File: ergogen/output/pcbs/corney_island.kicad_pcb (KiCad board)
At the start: 2 copper layers, 134.2 x 92.7 mm, 46 parts

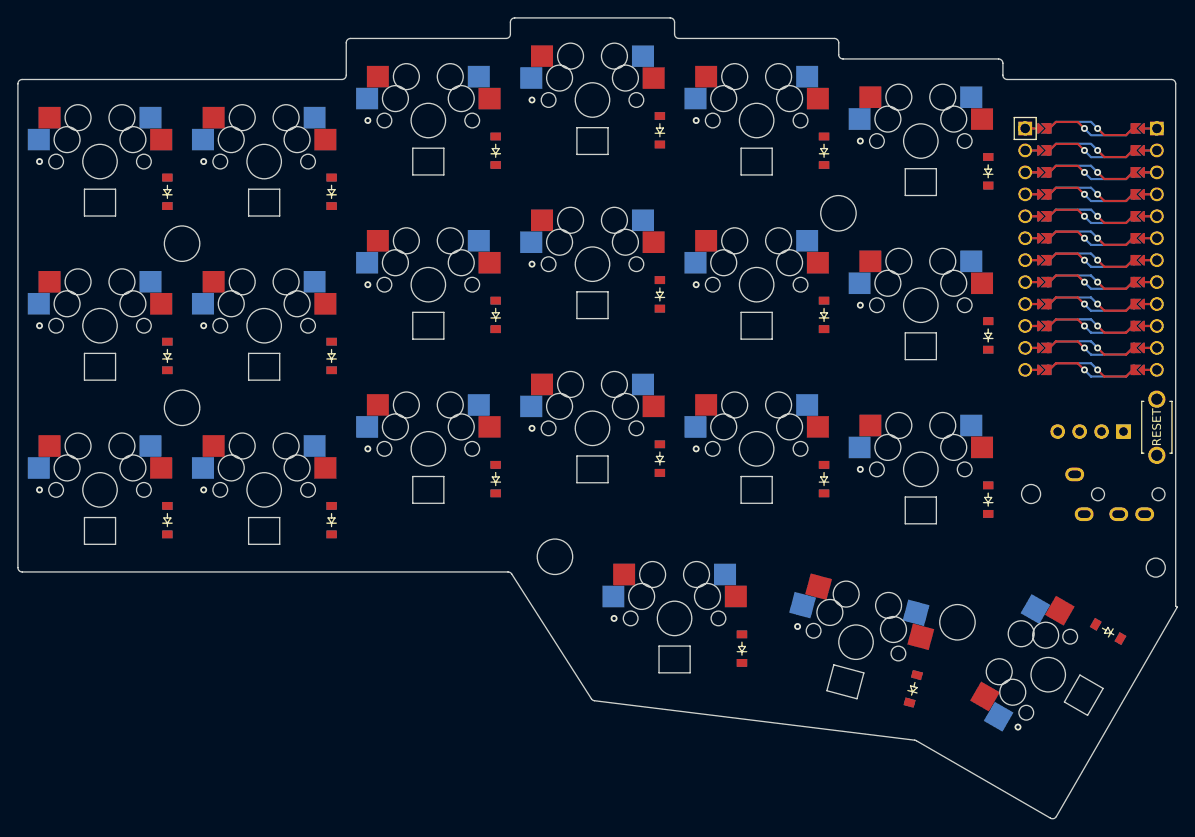
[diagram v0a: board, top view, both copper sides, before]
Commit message: Update nets and diode positions
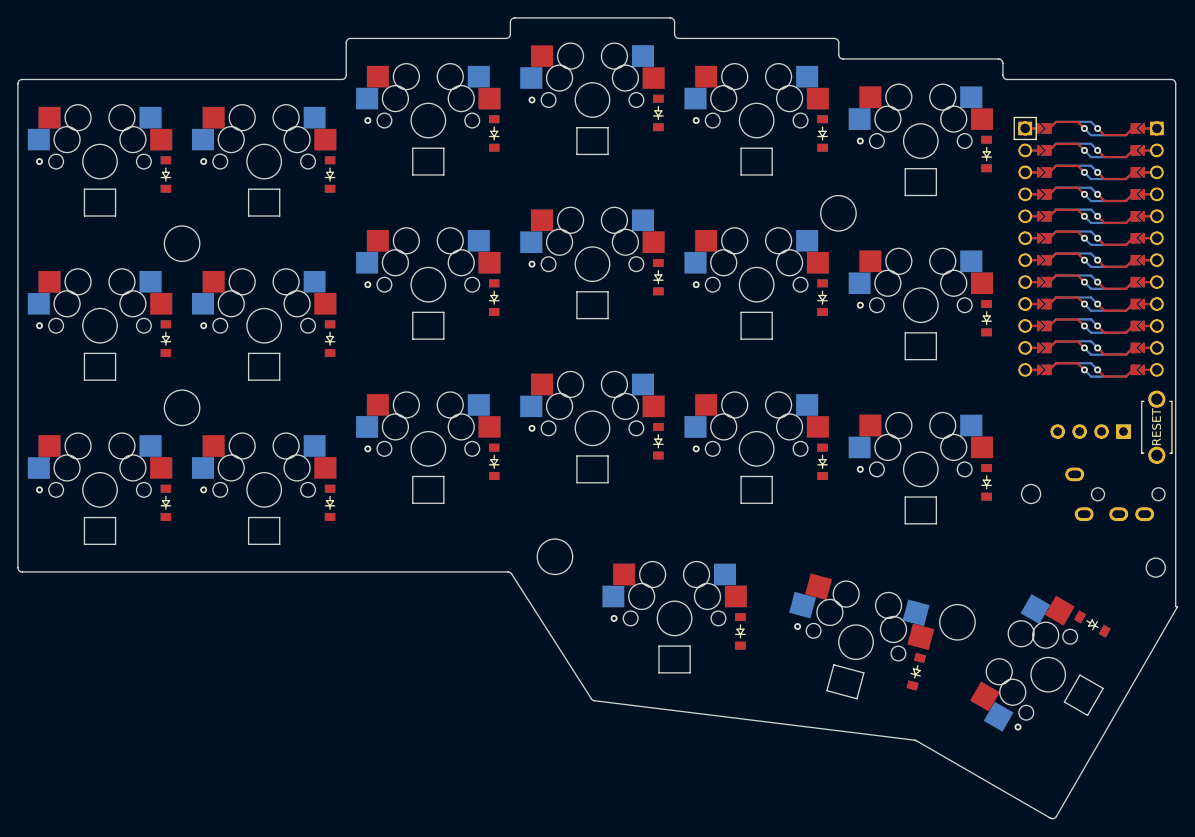
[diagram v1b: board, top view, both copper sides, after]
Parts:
- moved D21 2.01 mm to (214.9, 115.5)
- moved D1 2.01 mm to (107.6, 101.5)
- moved D10 2.01 mm to (164.6, 94.4)
- moved D11 2.01 mm to (164.6, 75.4)
- moved D12 2.01 mm to (164.6, 56.4)
- moved D13 2.01 mm to (183.6, 96.8)
- moved D14 2.01 mm to (183.6, 77.8)
- moved D15 2.01 mm to (183.6, 58.8)
- moved D16 2.01 mm to (202.6, 99.1)
- moved D17 2.01 mm to (202.6, 80.1)
- moved D18 2.01 mm to (202.6, 61.1)
- moved D19 2.01 mm to (174.1, 116.4)
- moved D2 2.01 mm to (107.6, 82.5)
- moved D3 2.01 mm to (107.6, 63.5)
- moved D4 2.01 mm to (126.6, 101.5)
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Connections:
- net P1 renamed LED
- D1 pad 1: R0 -> R2
- D10 pad 1: R0 -> R2
- D12 pad 1: R2 -> R0
- D13 pad 1: R0 -> R2
- D15 pad 1: R2 -> R0
- D16 pad 1: R0 -> R2
- D18 pad 1: R2 -> R0
- D3 pad 1: R2 -> R0
- D4 pad 1: R0 -> R2
- D6 pad 1: R2 -> R0
- D7 pad 1: R0 -> R2
- D9 pad 1: R2 -> R0

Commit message: Add per-key reversible LEDs
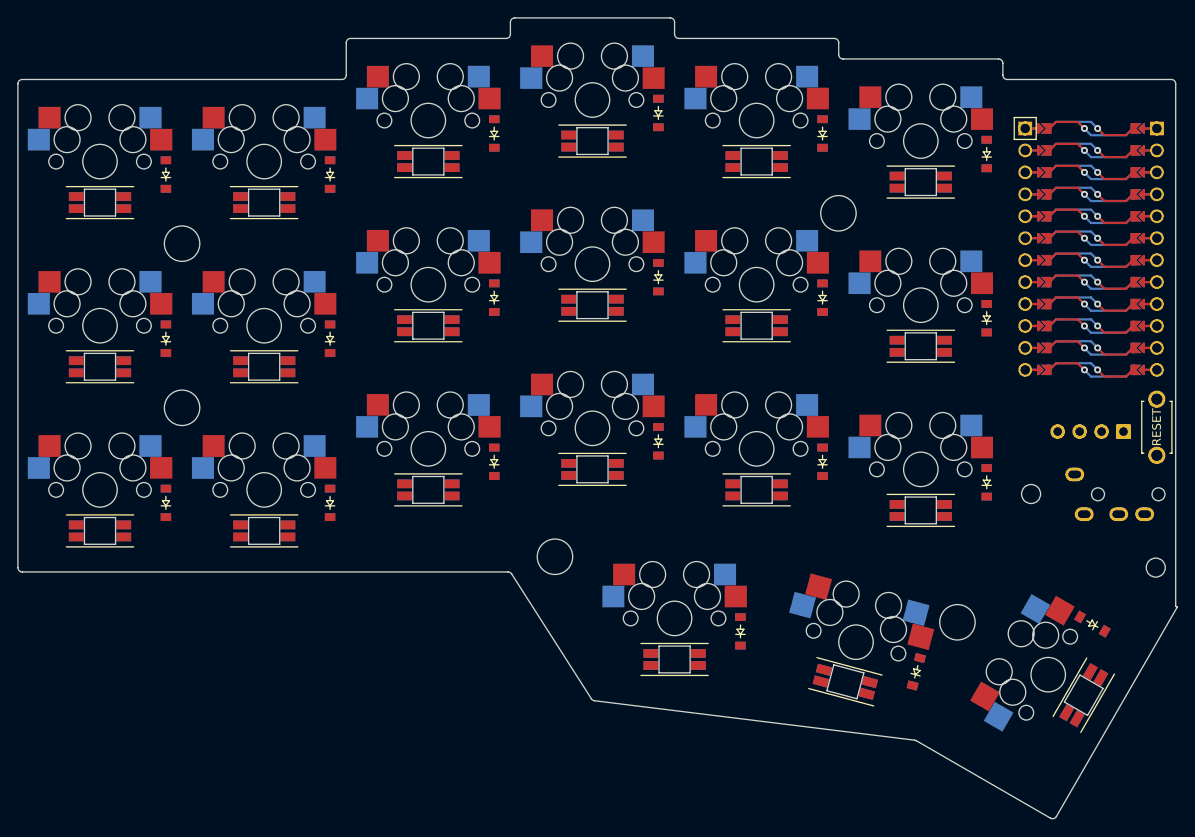
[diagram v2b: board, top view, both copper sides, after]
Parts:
- added LED1: YS-SK6812MINI-E, YS-SK6812MINI-E, F.Cu at (100.0, 104.8)
- added LED10: YS-SK6812MINI-E, YS-SK6812MINI-E, F.Cu at (157.0, 97.6)
- added LED11: YS-SK6812MINI-E, YS-SK6812MINI-E, F.Cu at (157.0, 78.6)
- added LED12: YS-SK6812MINI-E, YS-SK6812MINI-E, F.Cu at (157.0, 59.6)
- added LED13: YS-SK6812MINI-E, YS-SK6812MINI-E, F.Cu at (176.0, 100.0)
- added LED14: YS-SK6812MINI-E, YS-SK6812MINI-E, F.Cu at (176.0, 81.0)
- added LED15: YS-SK6812MINI-E, YS-SK6812MINI-E, F.Cu at (176.0, 62.0)
- added LED16: YS-SK6812MINI-E, YS-SK6812MINI-E, F.Cu at (195.0, 102.4)
- added LED17: YS-SK6812MINI-E, YS-SK6812MINI-E, F.Cu at (195.0, 83.4)
- added LED18: YS-SK6812MINI-E, YS-SK6812MINI-E, F.Cu at (195.0, 64.4)
- added LED19: YS-SK6812MINI-E, YS-SK6812MINI-E, F.Cu at (166.5, 119.6)
- added LED2: YS-SK6812MINI-E, YS-SK6812MINI-E, F.Cu at (100.0, 85.8)
- added LED20: YS-SK6812MINI-E, YS-SK6812MINI-E, F.Cu at (186.3, 122.2)
- added LED21: YS-SK6812MINI-E, YS-SK6812MINI-E, F.Cu at (213.9, 123.8)
- added LED3: YS-SK6812MINI-E, YS-SK6812MINI-E, F.Cu at (100.0, 66.8)
- added LED4: YS-SK6812MINI-E, YS-SK6812MINI-E, F.Cu at (119.0, 104.8)
- added LED5: YS-SK6812MINI-E, YS-SK6812MINI-E, F.Cu at (119.0, 85.8)
- added LED6: YS-SK6812MINI-E, YS-SK6812MINI-E, F.Cu at (119.0, 66.8)
- added LED7: YS-SK6812MINI-E, YS-SK6812MINI-E, F.Cu at (138.0, 100.0)
- added LED8: YS-SK6812MINI-E, YS-SK6812MINI-E, F.Cu at (138.0, 81.0)
- added LED9: YS-SK6812MINI-E, YS-SK6812MINI-E, F.Cu at (138.0, 62.0)
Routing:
- net C5: vias 5 -> 1
- net C4: vias 5 -> 1
- net C3: vias 5 -> 1
- net C2: vias 4 -> 1
- net C1: vias 4 -> 1
- net C0: vias 4 -> 1
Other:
- outline, holes or cut-outs redrawn

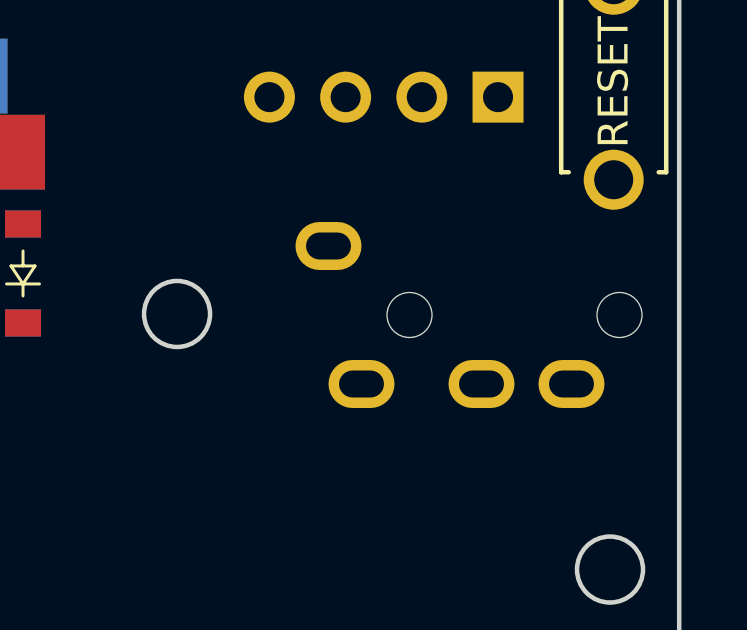
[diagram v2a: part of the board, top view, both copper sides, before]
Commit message: Switch to reversible TRRS jack
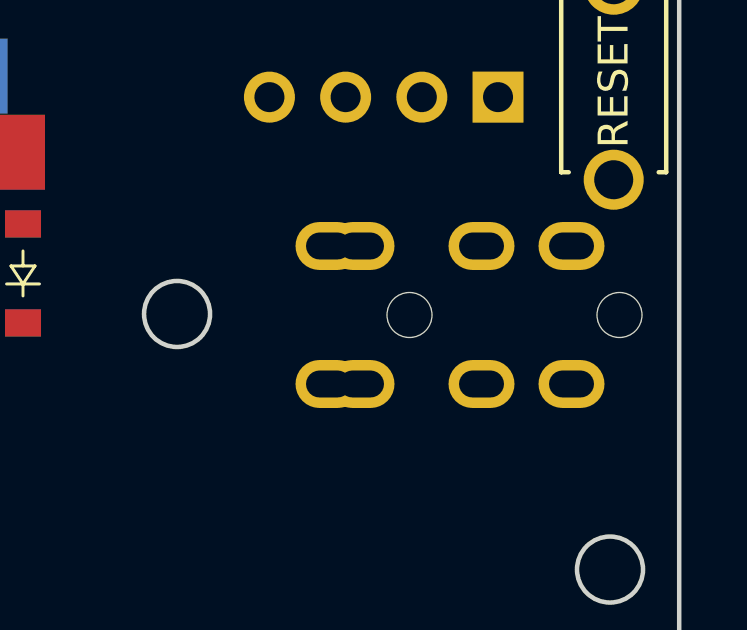
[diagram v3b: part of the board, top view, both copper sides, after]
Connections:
- TRRS1 pad 1: J1-PadA -> data
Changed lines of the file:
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@@
 (net 62 "P8")
 (net 63 "P9")
-(net 64 "J1-PadA")
   (net_class Default "This is the default net class."
     (clearance 0.2)
@@
 (add_net "P8")
 (add_net "P9")
-(add_net "J1-PadA")
   )
       (module MX (layer F.Cu)
@@
         (pad "" np_thru_hole circle (at -2.3 8.6) (size 1.5 1.5) (drill 1.5) (layers *.Cu *.Mask))
         (pad "" np_thru_hole circle (at -2.3 1.6) (size 1.5 1.5) (drill 1.5) (layers *.Cu *.Mask))
-        (pad 1 thru_hole oval (at -4.6 11.3 -90) (size 1.6 2.2) (drill oval 0.9 1.5) (layers *.Cu *.Mask) (net 64 "J1-PadA"))
+        (pad 1 thru_hole oval (at 0 11.3 -90) (size 1.6 2.2) (drill oval 0.9 1.5) (layers *.Cu *.Mask) (net 59 "data"))
+        (pad 2 thru_hole oval (at -4.6 10.2 -90) (size 1.6 2.2) (drill oval 0.9 1.5) (layers *.Cu *.Mask) (net 59 "data"))
+        (pad 3 thru_hole oval (at -4.6 6.2 -90) (size 1.6 2.2) (drill oval 0.9 1.5) (layers *.Cu *.Mask) (net 33 "GND"))
+        (pad 4 thru_hole oval (at -4.6 3.2 -90) (size 1.6 2.2) (drill oval 0.9 1.5) (layers *.Cu *.Mask) (net 31 "VCC"))
+        (pad 1 thru_hole oval (at -4.6 11.3 -90) (size 1.6 2.2) (drill oval 0.9 1.5) (layers *.Cu *.Mask) (net 59 "data"))
         (pad 2 thru_hole oval (at 0 10.2 -90) (size 1.6 2.2) (drill oval 0.9 1.5) (layers *.Cu *.Mask) (net 59 "data"))
         (pad 3 thru_hole oval (at 0 6.2 -90) (size 1.6 2.2) (drill oval 0.9 1.5) (layers *.Cu *.Mask) (net 33 "GND"))

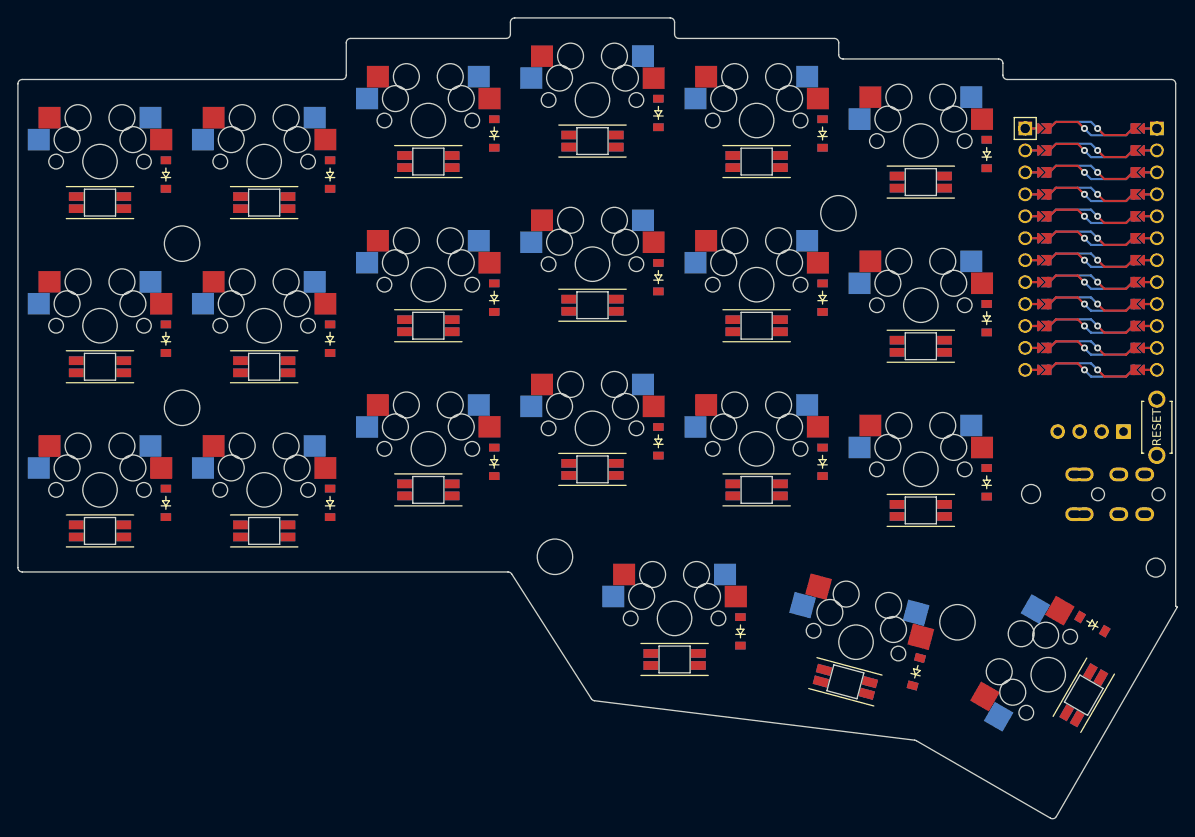
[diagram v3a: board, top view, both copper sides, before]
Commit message: Add LED and diode rotation, diode shift
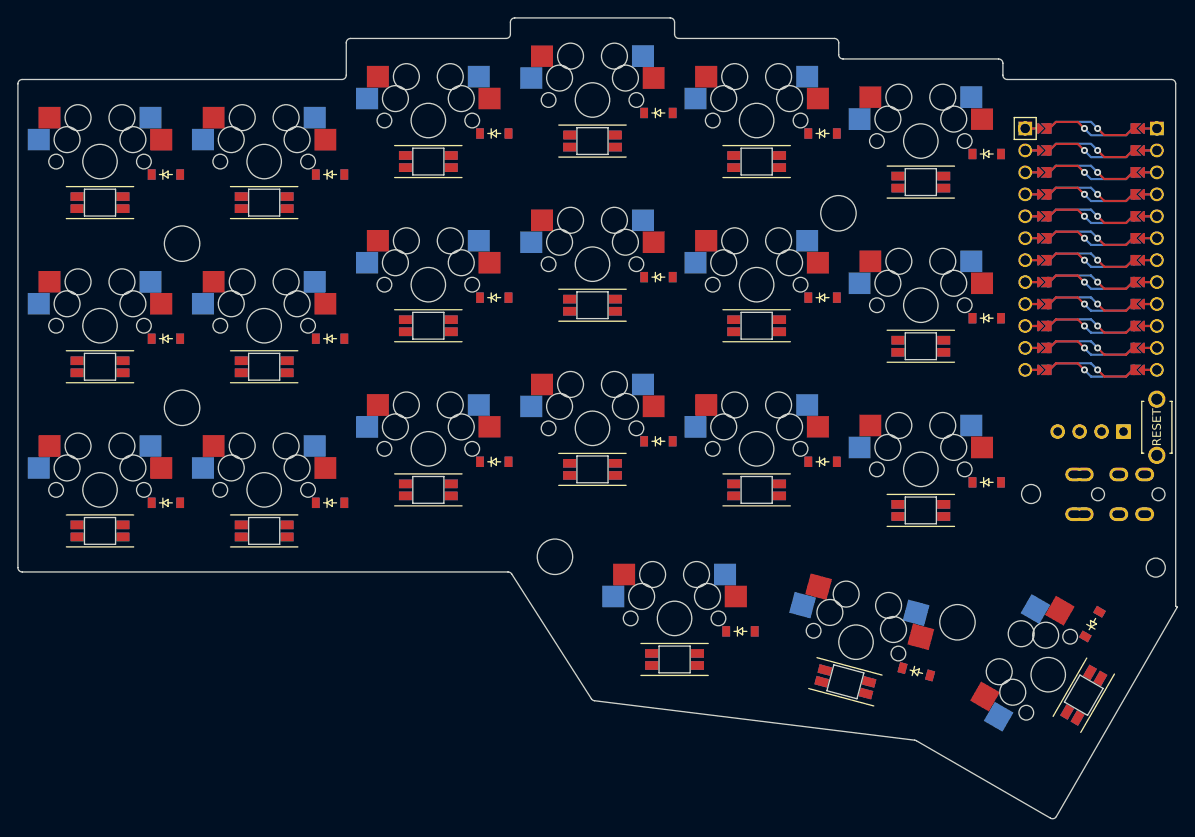
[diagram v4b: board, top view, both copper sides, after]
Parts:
- turned D1 to 0 degrees
- turned D10 to 0 degrees
- turned D11 to 0 degrees
- turned D12 to 0 degrees
- turned D13 to 0 degrees
- turned D14 to 0 degrees
- turned D15 to 0 degrees
- turned D16 to 0 degrees
- turned D17 to 0 degrees
- turned D18 to 0 degrees
- turned D19 to 0 degrees
- turned D2 to 0 degrees
- turned D20 to -15 degrees
- turned D21 to 60 degrees
- turned D3 to 0 degrees
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
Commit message: Fix missing diode rotation
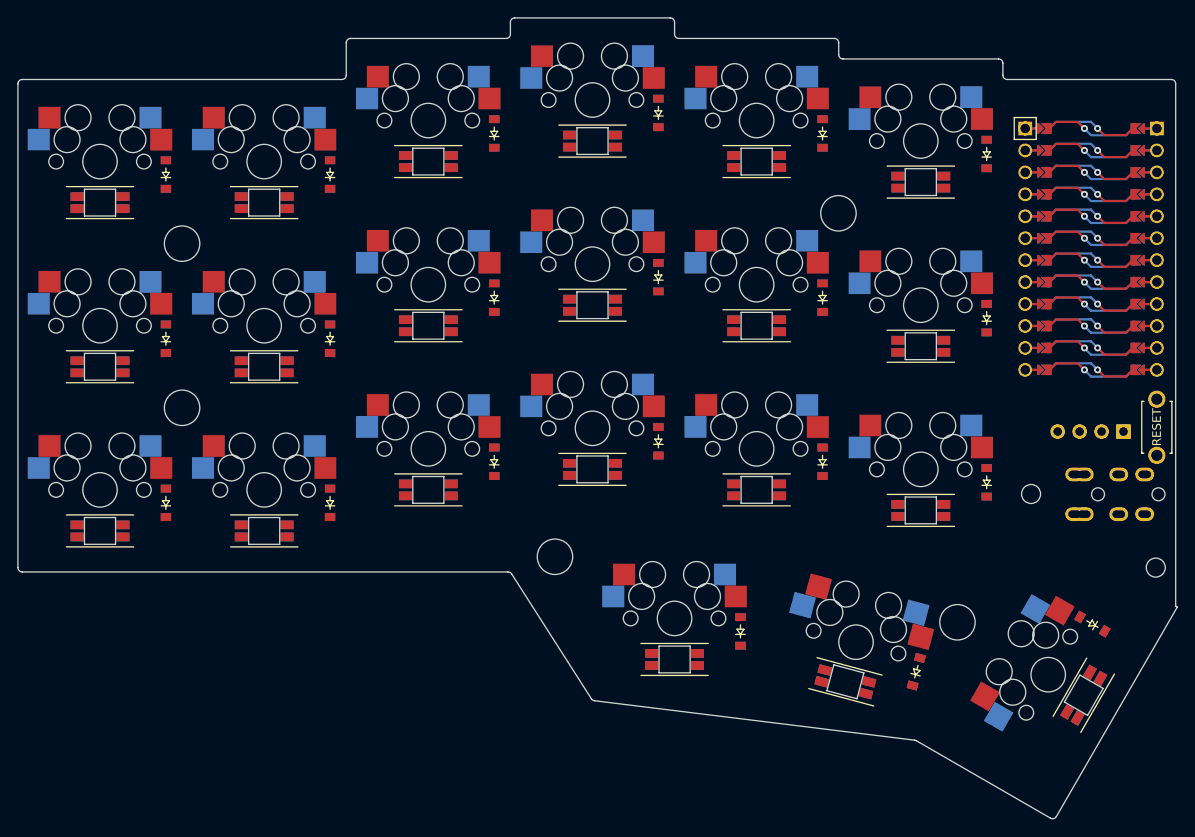
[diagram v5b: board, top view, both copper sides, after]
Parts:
- turned D1 to 90 degrees
- turned D10 to 90 degrees
- turned D11 to 90 degrees
- turned D12 to 90 degrees
- turned D13 to 90 degrees
- turned D14 to 90 degrees
- turned D15 to 90 degrees
- turned D16 to 90 degrees
- turned D17 to 90 degrees
- turned D18 to 90 degrees
- turned D19 to 90 degrees
- turned D2 to 90 degrees
- turned D20 to 75 degrees
- turned D21 to 150 degrees
- turned D3 to 90 degrees
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
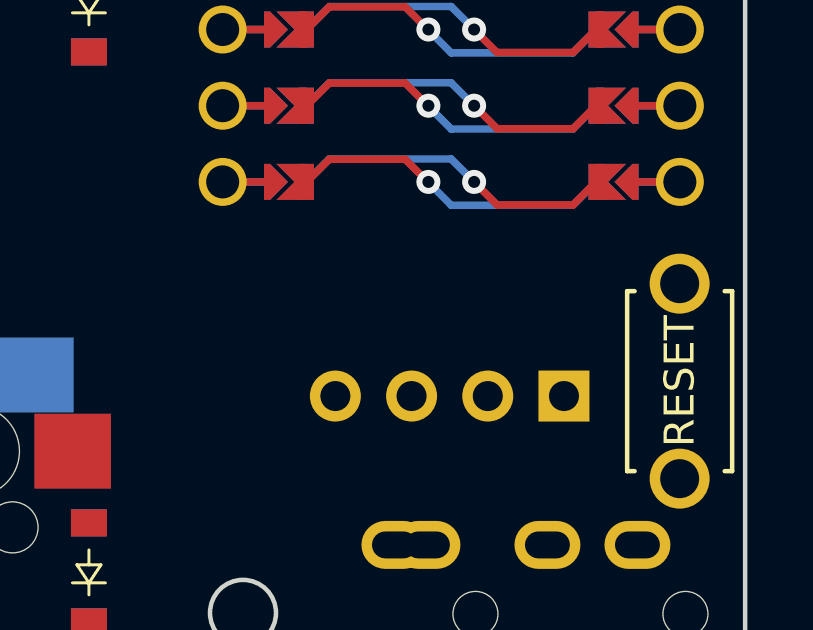
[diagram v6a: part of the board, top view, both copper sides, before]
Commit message: Update MCU pinouts
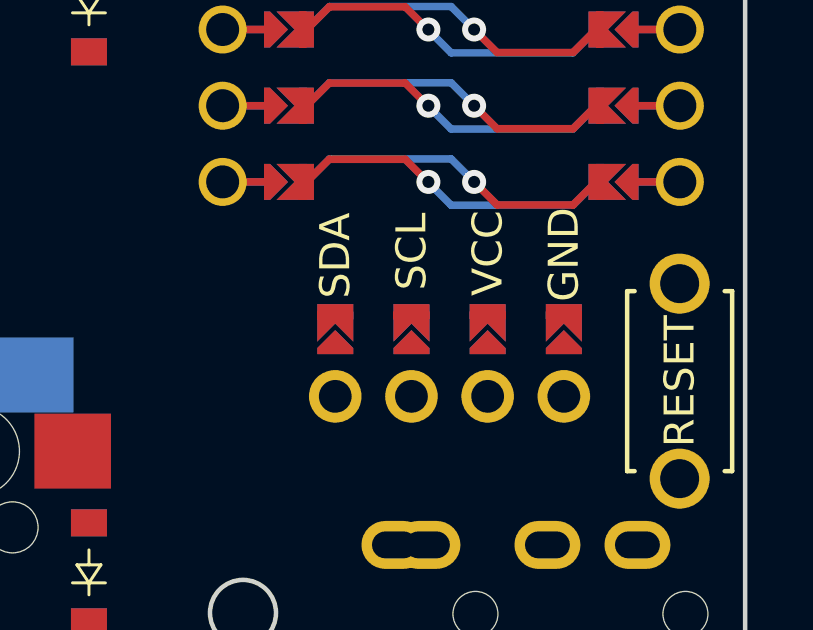
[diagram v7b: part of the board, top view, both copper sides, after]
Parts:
- removed OLED1: OLED, lib:OLED_headers
- added LED22: combined_oled, combined_oled, F.Cu at (214.6, 91.2)
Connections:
- net P16 renamed MOSI
- MCU1 pad 14: P8 -> R3
- MCU1 pad 15: R3 -> R2
- MCU1 pad 16: R2 -> R1
- MCU1 pad 17: R1 -> R0
- MCU1 pad 18: R0 -> CS
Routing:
- net P8: vias 1 -> 0
- net CS: vias 0 -> 1
